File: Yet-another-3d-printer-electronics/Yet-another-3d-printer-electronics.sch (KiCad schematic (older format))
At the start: 16 parts, among them CON1 SD_Card, P2 BEDTEMP, P3 ENDTEMP, P4 X-ENDSTOP, P5 Y-ENDSTOP, P6 Z-ENDSTOP, SW1 Switch_DPST, U2 LPC1114FBD48/302, X1 CRYSTAL_SMD

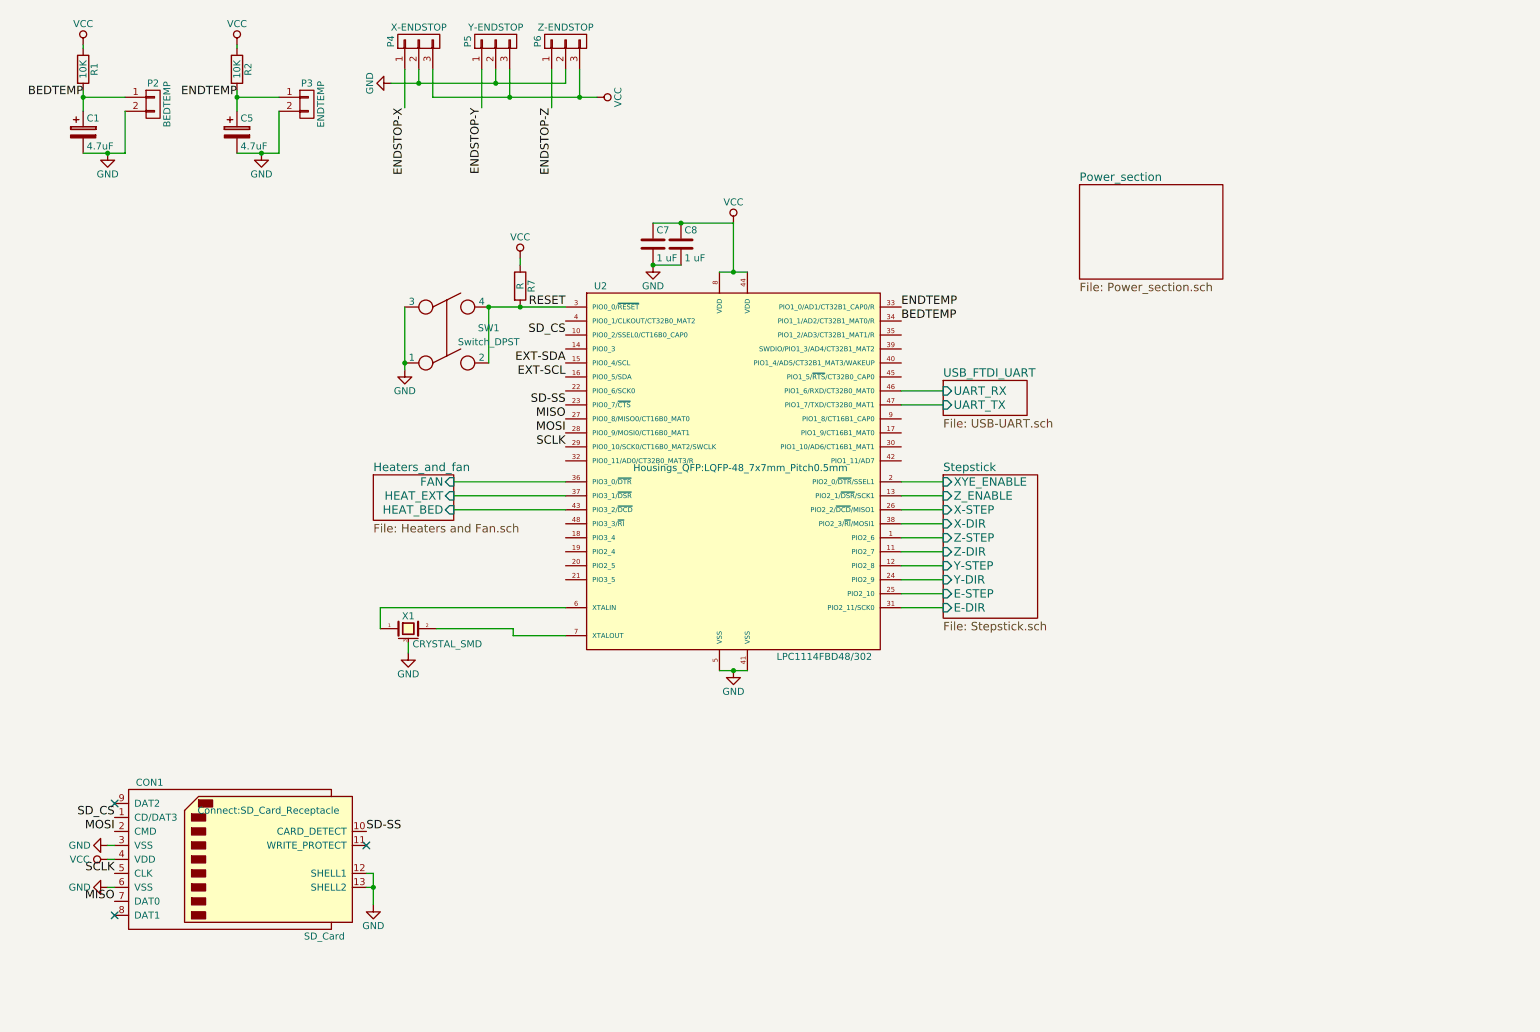
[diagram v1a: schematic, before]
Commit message: Redesign Endstops
Signed-off-by: Mateusz Krawczuk
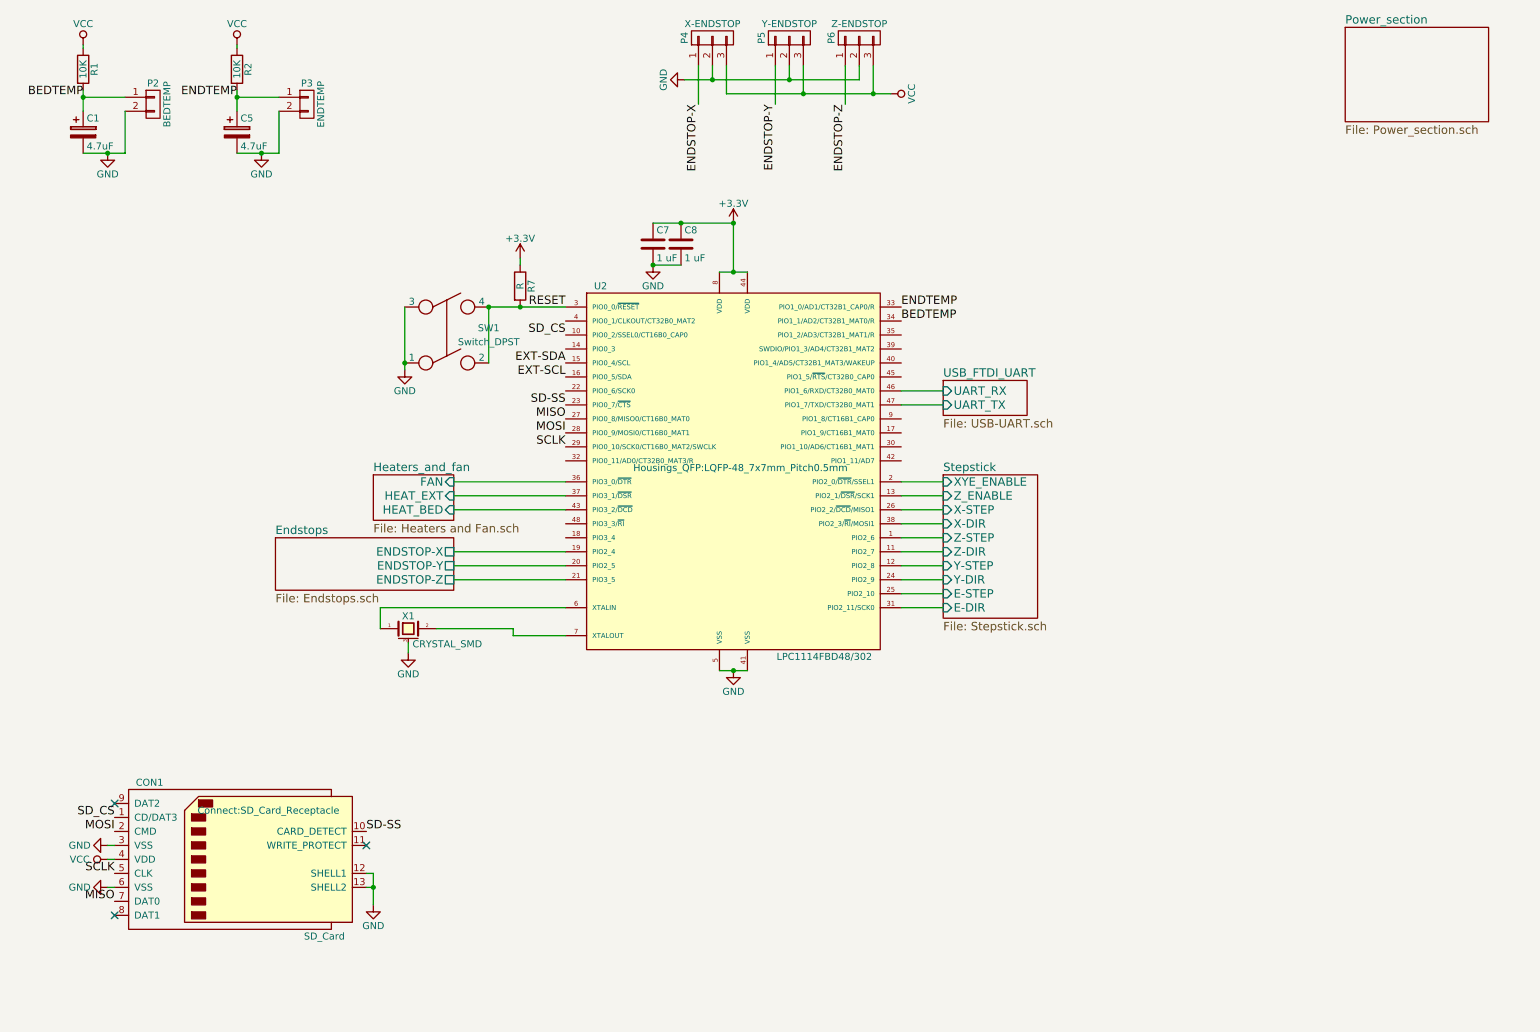
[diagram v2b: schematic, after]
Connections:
- net VCC: no longer C7.1, C8.1, R7.1, U2.44 (VDD), U2.8 (VDD)
- net Endstops/ENDSTOP-X: now reaches U2.19 (PIO2_4)
- net Endstops/ENDSTOP-Y: now reaches U2.20 (PIO2_5)
- net Endstops/ENDSTOP-Z: now reaches U2.21 (PIO3_5)
- new net +3V3: C7.1, C8.1, R7.1, U2.44 (VDD), U2.8 (VDD)
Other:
- moved on the sheet: P4, P5, P6
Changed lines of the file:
@@
 $Descr A4 11693 8268
 encoding utf-8
-Sheet 1 5
+Sheet 1 6
 Title "ZeroBoard - working title"
 Date "2017-02-24"
@@
 EXT-SDA
 $Comp
-L VCC #PWR02
-U 1 1 58834CC5
-P 5675 2025
-F 0 "#PWR02" H 5675 1875 50  0001 C CNN
-F 1 "VCC" H 5675 2175 50  0000 C CNN
-F 2 "" H 5675 2025 50  0000 C CNN
-F 3 "" H 5675 2025 50  0000 C CNN
-	1    5675 2025
-	1    0    0    -1
-$EndComp
-$Comp
 L C C8
 U 1 1 58834E5D
@@
 $EndComp
 $Comp
-L VCC #PWR05
-U 1 1 58865FDC
-P 4150 2275
-F 0 "#PWR05" H 4150 2125 50  0001 C CNN
-F 1 "VCC" H 4150 2425 50  0000 C CNN
-F 2 "" H 4150 2275 50  0000 C CNN
-F 3 "" H 4150 2275 50  0000 C CNN
-	1    4150 2275
-	1    0    0    -1
-$EndComp
-$Comp
 L Switch_DPST SW1
 U 1 1 58867A08
@@
 L CONN_01X03 P4
 U 1 1 588E7DA9
-P 3425 725
-F 0 "P4" H 3425 925 50  0000 C CNN
-F 1 "X-ENDSTOP" V 3525 725 50  0000 C CNN
-F 2 "Connectors_JST:JST_XH_B03B-XH-A_03x2.50mm_Straight" H 3425 725 50  0001 C CNN
-F 3 "" H 3425 725 50  0000 C CNN
-	1    3425 725
+P 5525 700
+F 0 "P4" H 5525 900 50  0000 C CNN
+F 1 "X-ENDSTOP" V 5625 700 50  0000 C CNN
+F 2 "Connectors_JST:JST_XH_B03B-XH-A_03x2.50mm_Straight" H 5525 700 50  0001 C CNN
+F 3 "" H 5525 700 50  0000 C CNN
+	1    5525 700
 	0    -1   -1   0
 $EndComp
@@
 L CONN_01X03 P5
 U 1 1 588E7EDF
-P 3975 725
-F 0 "P5" H 3975 925 50  0000 C CNN
-F 1 "Y-ENDSTOP" V 4075 725 50  0000 C CNN
-F 2 "Connectors_JST:JST_XH_B03B-XH-A_03x2.50mm_Straight" H 3975 725 50  0001 C CNN
-F 3 "" H 3975 725 50  0000 C CNN
-	1    3975 725
+P 6075 700
+F 0 "P5" H 6075 900 50  0000 C CNN
+F 1 "Y-ENDSTOP" V 6175 700 50  0000 C CNN
+F 2 "Connectors_JST:JST_XH_B03B-XH-A_03x2.50mm_Straight" H 6075 700 50  0001 C CNN
+F 3 "" H 6075 700 50  0000 C CNN
+	1    6075 700
 	0    -1   -1   0
 $EndComp
@@
 L CONN_01X03 P6
 U 1 1 588E7F5D
-P 4475 725
-F 0 "P6" H 4475 925 50  0000 C CNN
-F 1 "Z-ENDSTOP" V 4575 725 50  0000 C CNN
-F 2 "Connectors_JST:JST_XH_B03B-XH-A_03x2.50mm_Straight" H 4475 725 50  0001 C CNN
-F 3 "" H 4475 725 50  0000 C CNN
-	1    4475 725
+P 6575 700
+F 0 "P6" H 6575 900 50  0000 C CNN
+F 1 "Z-ENDSTOP" V 6675 700 50  0000 C CNN
+F 2 "Connectors_JST:JST_XH_B03B-XH-A_03x2.50mm_Straight" H 6575 700 50  0001 C CNN
+F 3 "" H 6575 700 50  0000 C CNN
+	1    6575 700
 	0    -1   -1   0
 $EndComp
@@
 L GND #PWR011
 U 1 1 588EBC43
-P 3225 1025
-F 0 "#PWR011" H 3225 775 50  0001 C CNN
-F 1 "GND" H 3225 875 50  0000 C CNN
-F 2 "" H 3225 1025 50  0000 C CNN
-F 3 "" H 3225 1025 50  0000 C CNN
-	1    3225 1025
+P 5325 1000
+F 0 "#PWR011" H 5325 750 50  0001 C CNN
+F 1 "GND" H 5325 850 50  0000 C CNN
+F 2 "" H 5325 1000 50  0000 C CNN
+F 3 "" H 5325 1000 50  0000 C CNN
+	1    5325 1000
 	0    1    1    0
 $EndComp
@@
 L VCC #PWR012
 U 1 1 588ECE1F
-P 4700 1125
-F 0 "#PWR012" H 4700 975 50  0001 C CNN
-F 1 "VCC" H 4700 1275 50  0000 C CNN
-F 2 "" H 4700 1125 50  0000 C CNN
-F 3 "" H 4700 1125 50  0000 C CNN
-	1    4700 1125
+P 6800 1100
+F 0 "#PWR012" H 6800 950 50  0001 C CNN
+F 1 "VCC" H 6800 1250 50  0000 C CNN
+F 2 "" H 6800 1100 50  0000 C CNN
+F 3 "" H 6800 1100 50  0000 C CNN
+	1    6800 1100
 	0    1    1    0
 $EndComp
-Text Label 3325 1200 3    60   ~ 0
+Text Label 5425 1175 3    60   ~ 0
 ENDSTOP-X
-Text Label 3875 1200 3    60   ~ 0
+Text Label 5975 1175 3    60   ~ 0
 ENDSTOP-Y
-Text Label 4375 1200 3    60   ~ 0
+Text Label 6475 1175 3    60   ~ 0
 ENDSTOP-Z
 NoConn ~ 3050 6475
@@
 	3050 6675 3100 6675
 Wire Wire Line
-	4375 925  4375 1200
-Wire Wire Line
-	3875 925  3875 1200
-Wire Wire Line
-	3325 925  3325 1200
-Connection ~ 4575 1125
-Connection ~ 4075 1125
-Wire Wire Line
-	3525 1125 4700 1125
-Connection ~ 3975 1025
-Connection ~ 3425 1025
-Wire Wire Line
-	3225 1025 4475 1025
-Wire Wire Line
-	4475 1025 4475 925
-Wire Wire Line
-	3975 1025 3975 925
-Wire Wire Line
-	3425 925  3425 1025
-Wire Wire Line
-	4575 1125 4575 925
-Wire Wire Line
-	4075 925  4075 1125
-Wire Wire Line
-	3525 925  3525 1125
+	6475 900  6475 1175
+Wire Wire Line
+	5975 900  5975 1175
+Wire Wire Line
+	5425 900  5425 1175
+Connection ~ 6675 1100
+Connection ~ 6175 1100
+Wire Wire Line
+	5625 1100 6800 1100
+Connection ~ 6075 1000
+Connection ~ 5525 1000
+Wire Wire Line
+	5325 1000 6575 1000
+Wire Wire Line
+	6575 1000 6575 900
+Wire Wire Line
+	6075 1000 6075 900
+Wire Wire Line
+	5525 900  5525 1000
+Wire Wire Line
+	6675 1100 6675 900
+Wire Wire Line
+	6175 900  6175 1100
+Wire Wire Line
+	5625 900  5625 1100
 Connection ~ 1025 1125
 Wire Wire Line
@@
 	3675 4075 4475 4075
 $Sheet
-S 8150 1750 1025 675
+S 10050 625  1025 675
 U 58B10119
 F0 "Power_section" 60
 F1 "Power_section.sch" 60
 $EndSheet
+$Comp
+L +3.3V #PWR?
+U 1 1 58FDAA0A
+P 5675 2025
+F 0 "#PWR?" H 5675 1875 50  0001 C CNN
+F 1 "+3.3V" H 5675 2165 50  0000 C CNN
+F 2 "" H 5675 2025 50  0001 C CNN
+F 3 "" H 5675 2025 50  0001 C CNN
+	1    5675 2025
+	1    0    0    -1
+$EndComp
+Connection ~ 5675 2025
+$Comp
+L +3.3V #PWR?
+U 1 1 58FDADD2
+P 4150 2275
+F 0 "#PWR?" H 4150 2125 50  0001 C CNN
+F 1 "+3.3V" H 4150 2415 50  0000 C CNN
+F 2 "" H 4150 2275 50  0001 C CNN
+F 3 "" H 4150 2275 50  0001 C CNN
+	1    4150 2275
+	1    0    0    -1
+$EndComp
+$Sheet
+S 2400 4275 1275 375
+U 58FE0CB7
+F0 "Endstops" 60
+F1 "Endstops.sch" 60
+F2 "ENDSTOP-X" U R 3675 4375 60
+F3 "ENDSTOP-Y" U R 3675 4475 60
+F4 "ENDSTOP-Z" U R 3675 4575 60
+$EndSheet
+Wire Wire Line
+	3675 4575 4475 4575
+Wire Wire Line
+	3675 4475 4475 4475
+Wire Wire Line
+	4475 4375 3675 4375
 $EndSCHEMATC

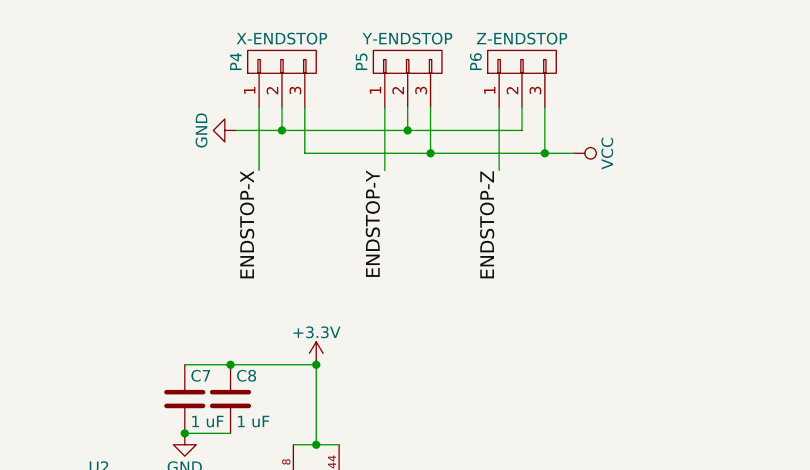
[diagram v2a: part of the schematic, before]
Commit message: Remove old enstops
Signed-off-by: Mateusz Krawczuk <mat.krawczuk@gmail.com>
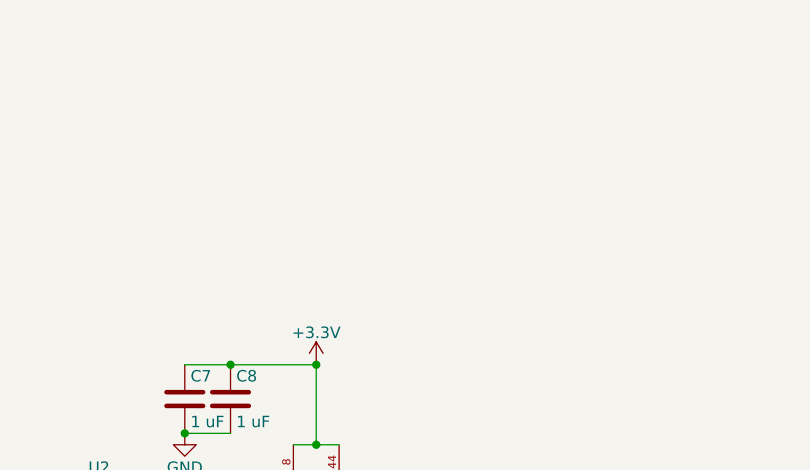
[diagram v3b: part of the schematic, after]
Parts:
- removed P4: X-ENDSTOP, Connectors_JST:JST_XH_B03B-XH-A_03x2.50mm_Straight, symbol CONN_01X03
- removed P5: Y-ENDSTOP, Connectors_JST:JST_XH_B03B-XH-A_03x2.50mm_Straight, symbol CONN_01X03
- removed P6: Z-ENDSTOP, Connectors_JST:JST_XH_B03B-XH-A_03x2.50mm_Straight, symbol CONN_01X03
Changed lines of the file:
@@
 Text Label 1025 1125 2    60   ~ 0
 BEDTEMP
-$Comp
-L CONN_01X03 P4
-U 1 1 588E7DA9
-P 5525 700
-F 0 "P4" H 5525 900 50  0000 C CNN
-F 1 "X-ENDSTOP" V 5625 700 50  0000 C CNN
-F 2 "Connectors_JST:JST_XH_B03B-XH-A_03x2.50mm_Straight" H 5525 700 50  0001 C CNN
-F 3 "" H 5525 700 50  0000 C CNN
-	1    5525 700
-	0    -1   -1   0
-$EndComp
-$Comp
-L CONN_01X03 P5
-U 1 1 588E7EDF
-P 6075 700
-F 0 "P5" H 6075 900 50  0000 C CNN
-F 1 "Y-ENDSTOP" V 6175 700 50  0000 C CNN
-F 2 "Connectors_JST:JST_XH_B03B-XH-A_03x2.50mm_Straight" H 6075 700 50  0001 C CNN
-F 3 "" H 6075 700 50  0000 C CNN
-	1    6075 700
-	0    -1   -1   0
-$EndComp
-$Comp
-L CONN_01X03 P6
-U 1 1 588E7F5D
-P 6575 700
-F 0 "P6" H 6575 900 50  0000 C CNN
-F 1 "Z-ENDSTOP" V 6675 700 50  0000 C CNN
-F 2 "Connectors_JST:JST_XH_B03B-XH-A_03x2.50mm_Straight" H 6575 700 50  0001 C CNN
-F 3 "" H 6575 700 50  0000 C CNN
-	1    6575 700
-	0    -1   -1   0
-$EndComp
-$Comp
-L GND #PWR011
-U 1 1 588EBC43
-P 5325 1000
-F 0 "#PWR011" H 5325 750 50  0001 C CNN
-F 1 "GND" H 5325 850 50  0000 C CNN
-F 2 "" H 5325 1000 50  0000 C CNN
-F 3 "" H 5325 1000 50  0000 C CNN
-	1    5325 1000
-	0    1    1    0
-$EndComp
-$Comp
-L VCC #PWR012
-U 1 1 588ECE1F
-P 6800 1100
-F 0 "#PWR012" H 6800 950 50  0001 C CNN
-F 1 "VCC" H 6800 1250 50  0000 C CNN
-F 2 "" H 6800 1100 50  0000 C CNN
-F 3 "" H 6800 1100 50  0000 C CNN
-	1    6800 1100
-	0    1    1    0
-$EndComp
-Text Label 5425 1175 3    60   ~ 0
-ENDSTOP-X
-Text Label 5975 1175 3    60   ~ 0
-ENDSTOP-Y
-Text Label 6475 1175 3    60   ~ 0
-ENDSTOP-Z
 NoConn ~ 3050 6475
 $Comp
@@
 Wire Wire Line
 	3050 6675 3100 6675
-Wire Wire Line
-	6475 900  6475 1175
-Wire Wire Line
-	5975 900  5975 1175
-Wire Wire Line
-	5425 900  5425 1175
-Connection ~ 6675 1100
-Connection ~ 6175 1100
-Wire Wire Line
-	5625 1100 6800 1100
-Connection ~ 6075 1000
-Connection ~ 5525 1000
-Wire Wire Line
-	5325 1000 6575 1000
-Wire Wire Line
-	6575 1000 6575 900
-Wire Wire Line
-	6075 1000 6075 900
-Wire Wire Line
-	5525 900  5525 1000
-Wire Wire Line
-	6675 1100 6675 900
-Wire Wire Line
-	6175 900  6175 1100
-Wire Wire Line
-	5625 900  5625 1100
 Connection ~ 1025 1125
 Wire Wire Line

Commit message: Add LCD Connector
Signed-off-by: Mateusz Krawczuk <mat.krawczuk@gmail.com>
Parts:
- added J?: LCD_Connector, symbol CONN_02X05
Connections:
- net GND: now also J?.10 (P10)
- net LCD_4: now reaches U2.17 (PIO1_9/CT16B1_MAT0)
- net LCD_4: now also J?.6 (P6)
- net LCD_Enable: now reaches U2.30 (PIO1_10/AD6/CT16B1_MAT1)
- net LCD_Enable: now also J?.4 (P4)
- net Encoder: now reaches U2.35 (PIO1_2/AD3/CT32B1_MAT1/R)
- net Encoder: now also J?.1 (P1)
- net LCD_RS: now reaches U2.39 (SWDIO/PIO1_3/AD4/CT32B1_MAT2)
- net LCD_RS: now also J?.3 (P3)
- net LCD_5: now reaches U2.40 (PIO1_4/AD5/CT32B1_MAT3/WAKEUP)
- net LCD_5: now also J?.5 (P5)
- net Buzzer: now reaches U2.42 (PIO1_11/AD7)
- net Buzzer: now also J?.2 (P2)
- net LCD_8: now reaches U2.45 (PIO1_5/~RTS~/CT32B0_CAP0)
- net LCD_8: now also J?.7 (P7)
- net LCD_6: now reaches U2.9 (PIO1_8/CT16B1_CAP0)
- net LCD_6: now also J?.8 (P8)
- new net +5V: J?.9 (P9)
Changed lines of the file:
@@
 Wire Wire Line
 	4475 4375 3675 4375
+$Comp
+L CONN_02X05 J?
+U 1 1 58FE5CD4
+P 9125 5700
+F 0 "J?" H 9125 6000 50  0000 C CNN
+F 1 "LCD_Connector" H 9175 5400 50  0000 C CNN
+F 2 "" H 9125 4500 50  0001 C CNN
+F 3 "" H 9125 4500 50  0001 C CNN
+	1    9125 5700
+	1    0    0    1
+$EndComp
+$Comp
+L +5V #PWR?
+U 1 1 58FE5EAC
+P 8800 5500
+F 0 "#PWR?" H 8800 5350 50  0001 C CNN
+F 1 "+5V" H 8800 5640 50  0000 C CNN
+F 2 "" H 8800 5500 50  0001 C CNN
+F 3 "" H 8800 5500 50  0001 C CNN
+	1    8800 5500
+	1    0    0    -1
+$EndComp
+$Comp
+L GND #PWR?
+U 1 1 58FE5F48
+P 9775 5500
+F 0 "#PWR?" H 9775 5250 50  0001 C CNN
+F 1 "GND" H 9775 5350 50  0000 C CNN
+F 2 "" H 9775 5500 50  0001 C CNN
+F 3 "" H 9775 5500 50  0001 C CNN
+	1    9775 5500
+	1    0    0    -1
+$EndComp
+Text Label 9375 5900 0    60   ~ 0
+Buzzer
+Text Label 8875 5900 2    60   ~ 0
+Encoder
+Text Label 9375 5800 0    60   ~ 0
+LCD_Enable
+Text Label 8875 5800 2    60   ~ 0
+LCD_RS
+Text Label 9375 5600 0    60   ~ 0
+LCD_6
+Text Label 9375 5700 0    60   ~ 0
+LCD_4
+Text Label 8875 5600 2    60   ~ 0
+LCD_8
+Text Label 8875 5700 2    60   ~ 0
+LCD_5
+Wire Wire Line
+	9375 5500 9775 5500
+Wire Wire Line
+	8875 5500 8800 5500
+Text Label 6875 2825 0    60   ~ 0
+Encoder
+Text Label 6875 2925 0    60   ~ 0
+LCD_RS
+Text Label 6875 3025 0    60   ~ 0
+LCD_5
+Text Label 6875 3125 0    60   ~ 0
+LCD_8
+Text Label 6875 3425 0    60   ~ 0
+LCD_6
+Text Label 6875 3525 0    60   ~ 0
+LCD_4
+Text Label 6875 3625 0    60   ~ 0
+LCD_Enable
+Text Label 6875 3725 0    60   ~ 0
+Buzzer
 $EndSCHEMATC

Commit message: Add User_Fan
Additional Mosfet for second Fan or LED strip.

Signed-off-by: Mateusz Krawczuk <mat.krawczuk@gmail.com>
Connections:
- net Heaters_and_fan/USER_FAN: now reaches U2.48 (PIO3_3/~RI~)
- no-connect marks 3 -> 8
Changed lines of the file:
@@
 	5575 5225 5775 5225
 $Sheet
-S 3100 3825 575  325
+S 3075 3825 600  400
 U 58B2ADB1
 F0 "Heaters_and_fan" 60
@@
 F3 "HEAT_EXT" I R 3675 3975 60
 F4 "FAN" I R 3675 3875 60
+F5 "USER_FAN" I R 3675 4175 60
 $EndSheet
 Wire Wire Line
@@
 $EndComp
 $Sheet
-S 2400 4275 1275 375
+S 2425 4325 1250 300
 U 58FE0CB7
 F0 "Endstops" 60
@@
 Text Label 6875 3725 0    60   ~ 0
 Buzzer
+Wire Wire Line
+	4475 4175 3675 4175
+NoConn ~ 4475 2725
+NoConn ~ 4475 2925
+NoConn ~ 4475 3725
+NoConn ~ 4475 4275
+NoConn ~ 4475 3225
 $EndSCHEMATC
